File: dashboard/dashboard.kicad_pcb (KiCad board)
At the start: 2 copper layers, 56 x 50 mm, 93 parts, among them J1 FUNC1_BTN, J10 PROG, J11 RGB, J12 5V_IN, J13 CAN, J14 PWR, J2 FUNC2_BTN, J3 FUNC3_BTN, J4 FAULT1_LED, J5 FAULT2_LED, J6 FAULT3_LED, J7 FUNC1_LED, J8 FUNC2_LED, J9 FUNC3_LED, Q1 2N7002, Q2 2N7002, Q3 2N7002, Q4 2N7002, Q5 2N7002, Q6 2N7002, SW1 SW_SPST, U1 FODM217D, U2 FODM217D, U3 FODM217D, U4 STM32F103C8Tx, U5 AP2204K-ADJ, U6 SN65HVD256D, U7 AP2204K-ADJ, Y1 8M, Y2 32.768k

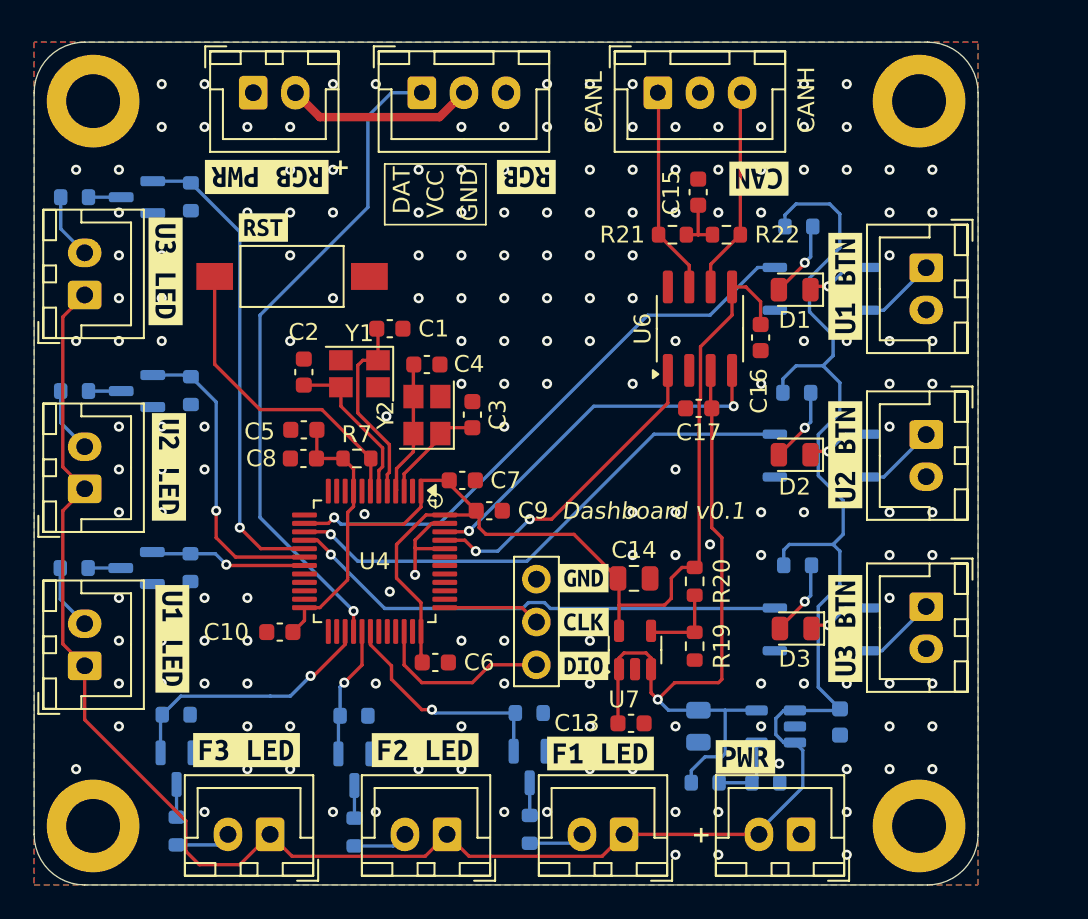
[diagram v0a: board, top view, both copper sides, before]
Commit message: fix: can jumper
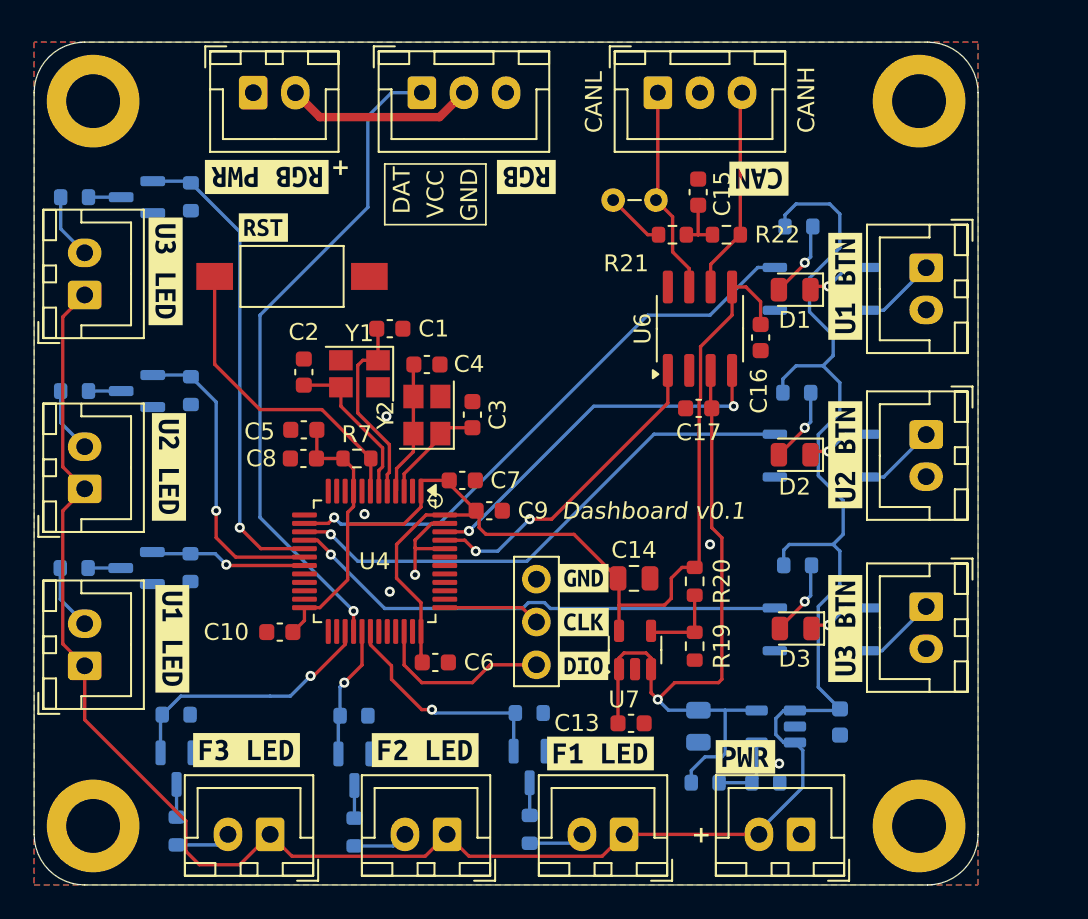
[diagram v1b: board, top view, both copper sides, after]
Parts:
- added JP1: J_CAN, PCM_Jumper_AKL:Jumper_P2.54mm_D0.7mm, F.Cu at (93.3, 54.4)
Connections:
- R21 pad 1: CAN_P -> Net-(JP1-A)
- U4 pad 45: Net-(U4-PB8) -> CRX
- U4 pad 46: Net-(U4-PB9) -> CTX
- U6 pad 1: Net-(U4-PB8) -> CTX
- U6 pad 4: Net-(U4-PB9) -> CRX
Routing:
- net (no net): track 0.00 -> 41.5 mm, vias 0 -> 4
- net Net-(U4-PB9): track 22.4 -> 0.00 mm, vias 2 -> 0
- net Net-(U4-PB8): track 19.1 -> 0.00 mm, vias 2 -> 0
- net Net-(JP1-A): track 0.00 -> 3.55 mm
- net GND: vias 176 -> 6

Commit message: fix: dashboard CAN
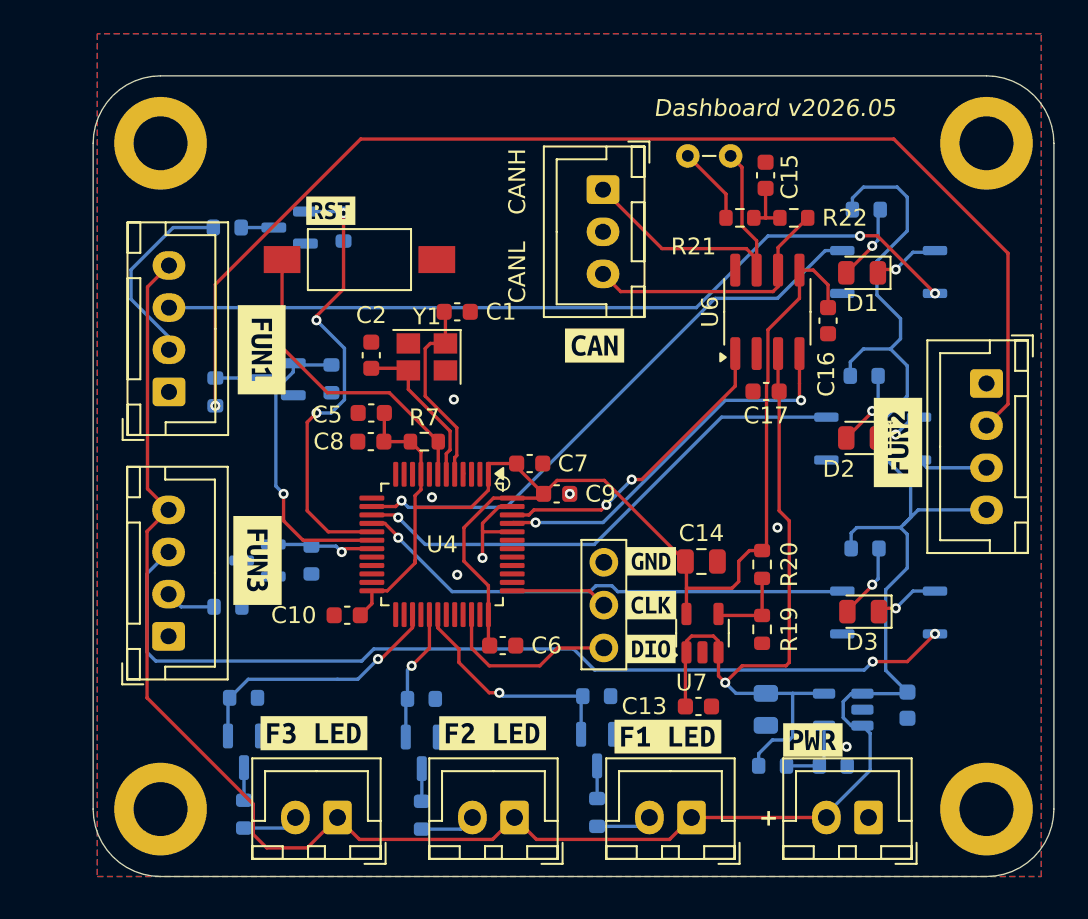
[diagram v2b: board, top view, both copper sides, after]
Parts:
- removed C3, C4: 20p, Capacitor_SMD:C_0603_1608Metric
- removed J11: RGB, Connector_JST:JST_XH_B3B-XH-A_1x03_P2.50mm_Vertical
- removed J12: 5V_IN, Connector_JST:JST_XH_B2B-XH-A_1x02_P2.50mm_Vertical
- removed J7: FUNC1_LED, Connector_JST:JST_XH_B2B-XH-A_1x02_P2.50mm_Vertical
- removed J8: FUNC2_LED, Connector_JST:JST_XH_B2B-XH-A_1x02_P2.50mm_Vertical
- removed J9: FUNC3_LED, Connector_JST:JST_XH_B2B-XH-A_1x02_P2.50mm_Vertical
- removed Y2: 32.768k, Crystal:Crystal_SMD_SeikoEpson_FA238-4Pin_3.2x2.5mm
- removed kibuzzard-675A93D8: G***, kibuzzard-675A93D8
- removed kibuzzard-675A93DE: G***, kibuzzard-675A93DE
- removed kibuzzard-675A93E3: G***, kibuzzard-675A93E3
- removed kibuzzard-675A9409: G***, kibuzzard-675A9409
- removed kibuzzard-675A9410: G***, kibuzzard-675A9410
- removed kibuzzard-675A9417: G***, kibuzzard-675A9417
- removed kibuzzard-675A942D: G***, kibuzzard-675A942D
- removed kibuzzard-675A9464: G***, kibuzzard-675A9464
- added kibuzzard-6A0E8E86: G***, kibuzzard-6A0E8E86, F.Cu at (110.2, 68.8)
- added kibuzzard-6A0E8E93: G***, kibuzzard-6A0E8E93, F.Cu at (72.5, 63.2)
- added kibuzzard-6A0E8E9D: G***, kibuzzard-6A0E8E9D, F.Cu at (72.2, 75.8)
- J1: value FUNC1_BTN -> Func1; footprint Connector_JST:JST_XH_B2B-XH-A_1x02_P2.50mm_Vertical -> Connector_JST:JST_XH_B4B-XH-A_1x04_P2.50mm_Vertical
- J2: value FUNC2_BTN -> Func1; footprint Connector_JST:JST_XH_B2B-XH-A_1x02_P2.50mm_Vertical -> Connector_JST:JST_XH_B4B-XH-A_1x04_P2.50mm_Vertical
- J3: value FUNC3_BTN -> Func1; footprint Connector_JST:JST_XH_B2B-XH-A_1x02_P2.50mm_Vertical -> Connector_JST:JST_XH_B4B-XH-A_1x04_P2.50mm_Vertical
- moved J1 45.5 mm to (67.0, 65.8), turned to 90 degrees
- moved J3 45.0 mm to (67.0, 80.2), turned to 90 degrees
- moved kibuzzard-675A946D 13.9 mm to (92.2, 63.0), turned to 0 degrees
- moved R16 9.41 mm to (70.5, 78.5)
- moved R11 9.23 mm to (77.4, 56.0)
- moved Q4 9.23 mm to (74.2, 56.0)
- moved R12 9.23 mm to (70.5, 56.0)
- moved Q5 8.37 mm to (73.4, 65.0)
- moved R13 8.37 mm to (76.6, 65.0)
- moved R14 8.35 mm to (69.8, 65.8), turned to 90 degrees
- moved Q6 7.19 mm to (72.2, 75.8)
- moved R15 7.19 mm to (75.5, 75.7)
- moved J13 6.60 mm to (92.8, 53.8), turned to -90 degrees
- moved JP1 5.15 mm to (97.8, 51.8)
- moved H1 4.72 mm to (66.5, 51.0)
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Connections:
- J1 pad 1: Net-(J1-Pin_1) -> GND
- J1 pad 2: GND -> Func1_led
- J13 pad 2: unconnected-(J13-Pin_2-Pad2) -> GND
- J2 pad 1: Net-(J2-Pin_1) -> GND
- J2 pad 2: GND -> Func2_led
- J3 pad 1: Net-(J3-Pin_1) -> GND
- J3 pad 2: GND -> Func3_led
- R12 pad 1: Net-(J7-Pin_2) -> Func1_led
- R14 pad 1: Net-(J8-Pin_2) -> Func2_led
- R16 pad 1: Net-(J9-Pin_2) -> Func3_led
- U1 pad 2: Net-(J1-Pin_1) -> func1_rst
- U2 pad 2: Net-(J2-Pin_1) -> func2_rst
- U3 pad 2: Net-(J3-Pin_1) -> func3_rst
- U4 pad 2: ADC_CH1 -> unconnected-(U4-PC13-Pad2)
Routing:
- net Func2_led: track 0.00 -> 71.4 mm, vias 0 -> 1
- net func3_rst: track 0.00 -> 55.1 mm, vias 0 -> 2
- net func1_rst: track 0.00 -> 48.6 mm, vias 0 -> 2
- net (no net): track 41.5 -> 0.00 mm, vias 4 -> 0
- net RGB: track 39.3 -> 0.00 mm, vias 1 -> 0
- net CRX: track 0.00 -> 23.0 mm, vias 0 -> 2
- net CTX: track 0.00 -> 18.3 mm, vias 0 -> 2
- net Func1_led: track 0.00 -> 11.6 mm
- net Net-(J11-Pin_2): track 11.2 -> 0.00 mm
- net /LSE_OUT: track 7.96 -> 0.07 mm
- net CAN_P: track 12.5 -> 18.9 mm
- net /LSE_IN: track 6.35 -> 0.00 mm
- net VDC: track 133.8 -> 139.4 mm
- net Net-(J3-Pin_1): track 4.56 -> 0.00 mm
- net Net-(J2-Pin_1): track 4.52 -> 0.00 mm
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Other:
- board size 56 x 50 mm -> 57 x 47.5 mm
- board text added: "Dashboard v2026.05"
- board text removed: "DAT"
- board text removed: "Dashboard v0.1"
- board text removed: "GND"
- board text removed: "VCC"
